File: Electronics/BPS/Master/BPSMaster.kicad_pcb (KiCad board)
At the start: 2 copper layers, 100 x 75 mm, 185 parts, among them J1 SWD, J10 DisplayJumper, J11 FrontFans, J12 BackFans, J13 ErrorLightConnector, J2 Logic Analyzer, J20 USBConnector, J21 USB_B_Micro, J3 CurrentSlaveConnector, J4 CarPowerConnector, J5 CAN_Out, J6 ContactorConnector, J7 VoltageSlaveConnector, J8 DisplayConnector, J9 TempSlaveConnector, Q1 VND5N07-E, Q2 NVR4003NT3G, Q3 NVR4003NT3G, Q4 NVR4003NT3G, SW1 B3SL-1002P, U1 STM32F413RHTx, U10 LTC6820, U11 HX1188FNL, U12 LTC6820, U13 Si8641EC-B-IS1, U14 SI8660EC-B-IS1, U15 RI3-1205S, U16 SI8261ABC-IS, U17 CP2102N-A01-GQFN24, U2 RI3-1205S, U3 NCP1117-3.3_SOT223, U4 CDSOT23-T24CAN, U5 ADM3055E, U6 BAS70-04, U7 SI8261ABC-IS, U8 M24128, U9 LSM6DS3, Y1 NX8045GB-8.000M-STD-CSJ-1

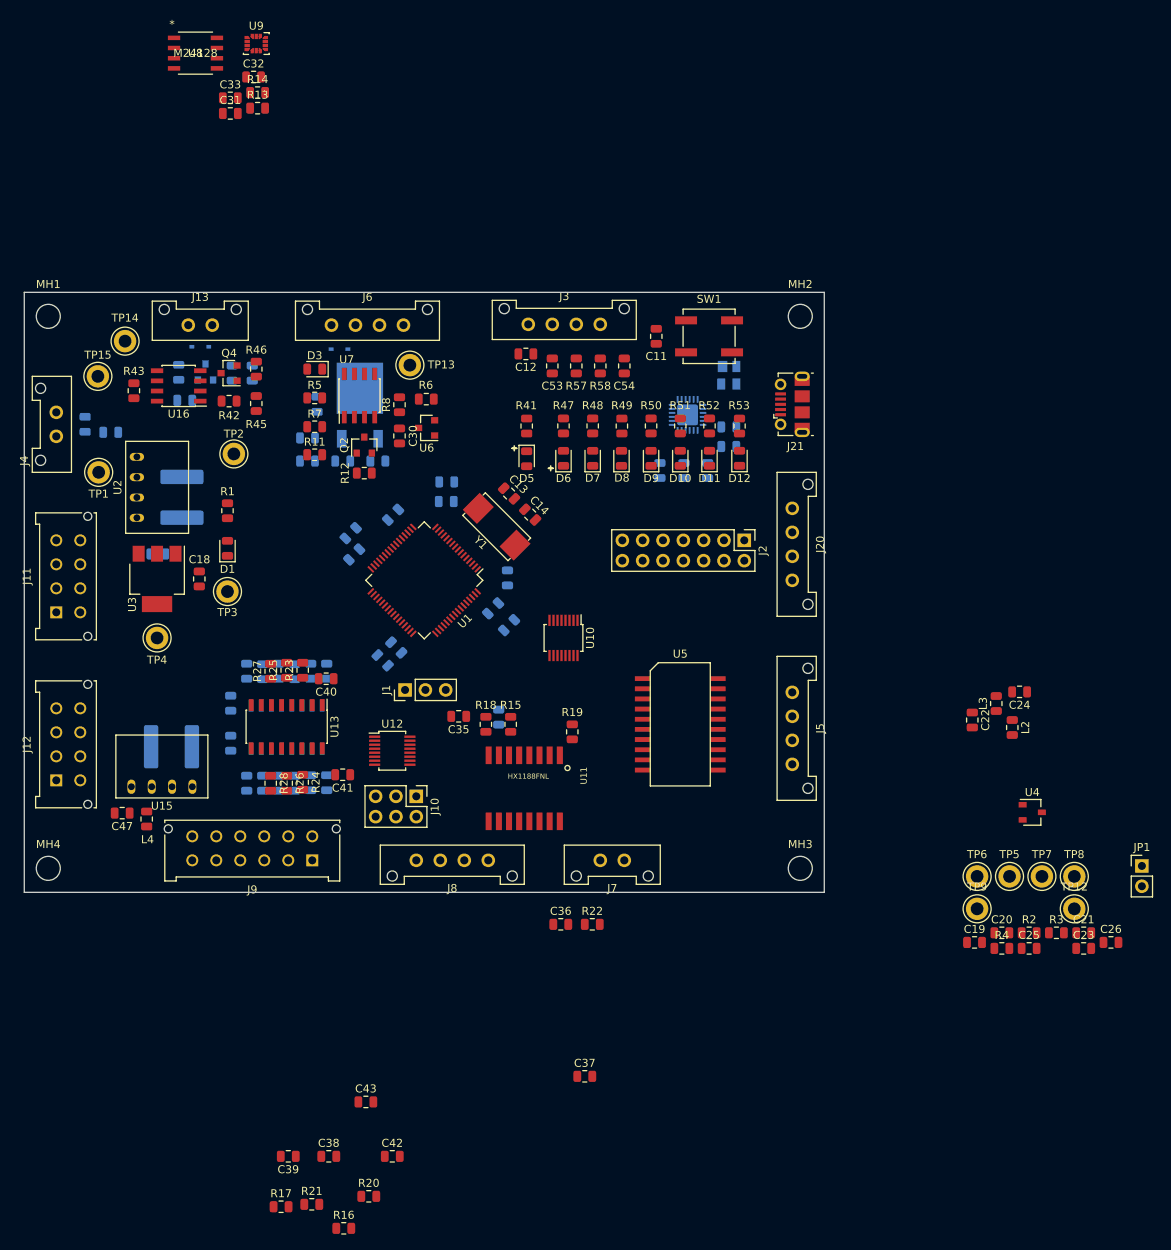
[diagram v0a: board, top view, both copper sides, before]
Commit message: Organized all components in BPS master to where they should be.
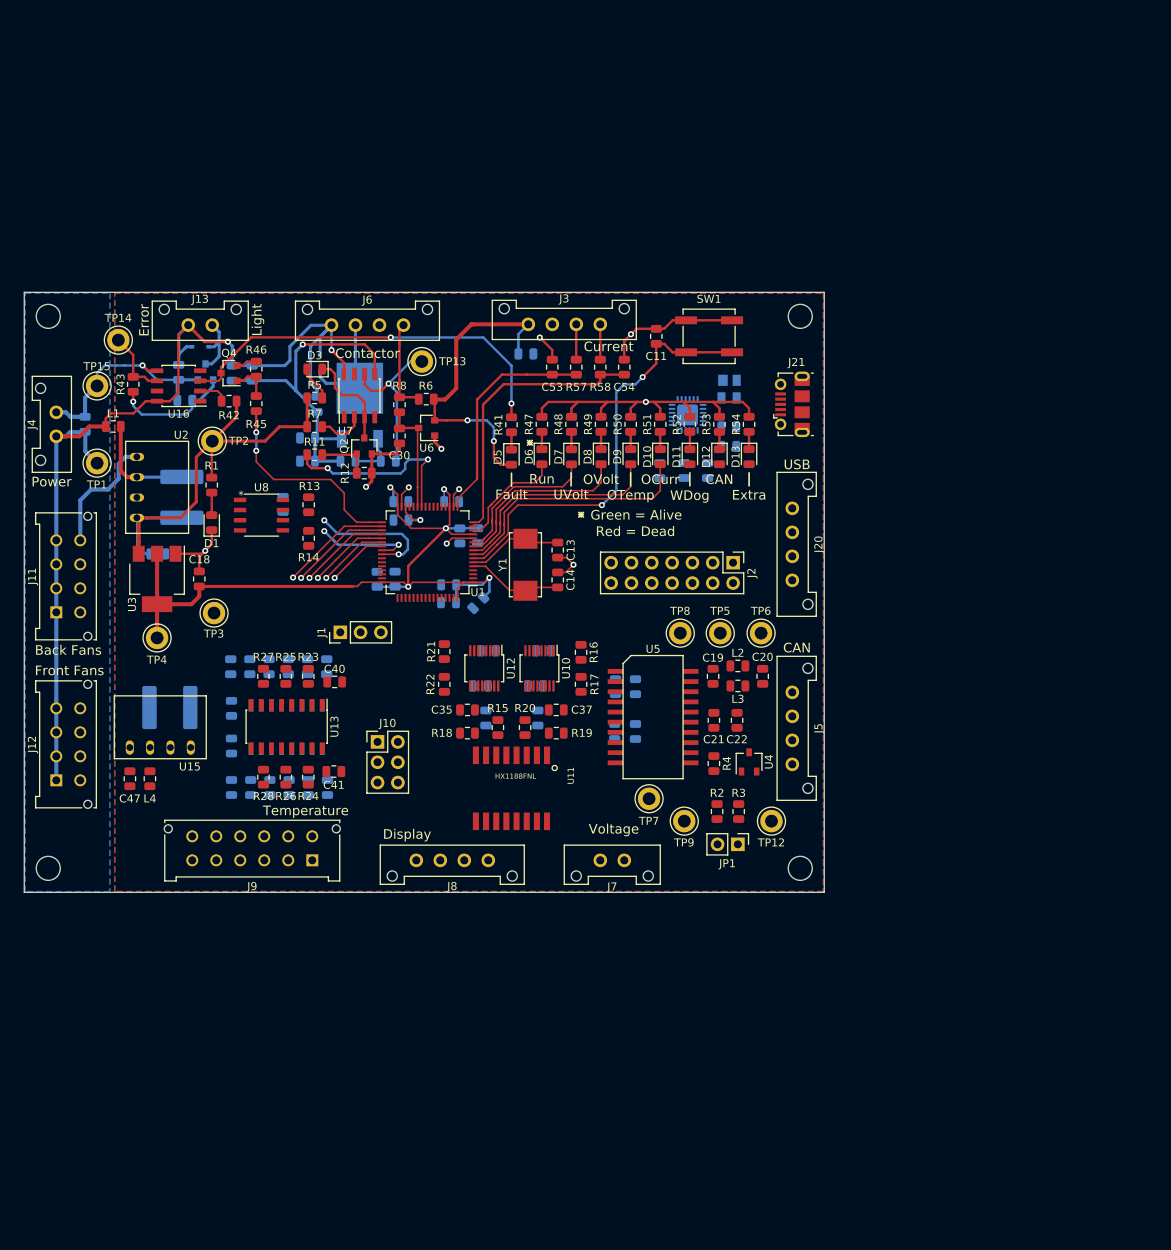
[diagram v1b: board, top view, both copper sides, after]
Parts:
- removed C32, C33: 0.1uF, Capacitor_SMD:C_0805_2012Metric
- removed U9: LSM6DS3, Package_LGA:LGA-14_3x2.5mm_P0.5mm_LayoutBorder3x4y
- added D14: SP0503BAHT, Package_TO_SOT_SMD:SOT-143, B.Cu at (188.1, 87.1)
- added R59: 1k, Resistor_SMD:R_0805_2012Metric, B.Cu at (179.4, 97.3)
- C12, C23, C24, C25, C26, C31, C36, C38, C39, C42, C43: moved to B.Cu
- D13: value SP0503BAHT -> Extra; footprint Package_TO_SOT_SMD:SOT-143 -> LED_SMD:LED_0805_2012Metric; moved to F.Cu
- D7: value OVolt -> UVolt
- D8: value UVolt -> OVolt
- L1: moved to F.Cu
- R54: value 1k -> 750; moved to F.Cu
- moved R16 77.9 mm to (169.6, 120.0), turned to 90 degrees
- moved R17 75.3 mm to (169.6, 124.0), turned to 90 degrees
- moved R21 71.1 mm to (152.5, 119.9), turned to 90 degrees
- moved C26 67.4 mm to (173.8, 129.9), turned to 270 degrees
- moved C23 67.0 mm to (173.9, 124.3), turned to 90 degrees
- moved C42 64.3 mm to (158.0, 119.8)
- moved C39 63.1 mm to (164.2, 128.2), turned to 90 degrees
- moved C38 61.8 mm to (157.0, 124.2)
- moved R20 61.8 mm to (162.6, 129.4), turned to 90 degrees
- moved U8 58.3 mm to (129.7, 102.8)
- moved TP8 57.9 mm to (182.0, 117.6)
- moved C25 56.2 mm to (176.4, 129.9), turned to 270 degrees
- moved C43 56.2 mm to (163.9, 124.2)
- moved R14 56.1 mm to (135.6, 105.8), turned to 90 degrees
- moved C21 53.3 mm to (186.2, 128.5), turned to 270 degrees
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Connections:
- net /CAN/GND_ISO_IN renamed Net-(C20-Pad2)
- net /CAN/GND_ISO_OUT renamed Net-(C19-Pad2)
- C19 pad 1: /CAN/CAN_ISA_VOUT -> Net-(C19-Pad1)
- C20 pad 1: /CAN/CAN_ISA_VOUT -> Net-(C20-Pad1)
- C21 pad 1: /CAN/CAN_ISA_VOUT -> Net-(C20-Pad1)
- C22 pad 1: /CAN/CAN_ISA_VOUT -> Net-(C20-Pad1)
- C30 pad 1: /PC7 -> /PB1
- C53 pad 1: /ADC1_CH2 -> /ADC1_CH3
- C54 pad 1: /ADC1_CH3 -> /ADC1_CH2
- D10 pad 1: GND -> Net-(D10-Pad1)
- D10 pad 2: Net-(D10-Pad2) -> /PC0
- D11 pad 1: GND -> Net-(D11-Pad1)
- D11 pad 2: Net-(D11-Pad2) -> /PA5
- D12 pad 1: GND -> Net-(D12-Pad1)
- D12 pad 2: Net-(D12-Pad2) -> /PA6
- D13 pad 1: GND -> Net-(D13-Pad1)
- D13 pad 2: /USB/VBUS -> /PA7
- D6 pad 1: GND -> Net-(D6-Pad1)
- D6 pad 2: Net-(D6-Pad2) -> /RUN
- D7 pad 1: GND -> Net-(D7-Pad1)
- D7 pad 2: Net-(D7-Pad2) -> /PC3
- D8 pad 1: GND -> Net-(D8-Pad1)
- D8 pad 2: Net-(D8-Pad2) -> /PC2
- D9 pad 1: GND -> Net-(D9-Pad1)
- D9 pad 2: Net-(D9-Pad2) -> /PC1
- J10 pad 2: /SPI/DISP_POL -> +3V3
- J10 pad 3: GND -> /SPI/DISP_POL
- J10 pad 4: +3V3 -> /SPI/DISP_PHA
- J10 pad 5: /SPI/DISP_PHA -> GND
- J5 pad 1: /CAN/CAN_ISA_VOUT -> Net-(C20-Pad1)
- J8 pad 1: +12V -> Net-(J8-Pad1)
- J8 pad 2: GNDPWR -> Net-(J8-Pad2)
- J8 pad 3: Net-(J8-Pad3) -> +12V
- J8 pad 4: Net-(J8-Pad4) -> GNDPWR
- J9 pad 5: Net-(J9-Pad5) -> GND_A
- L2 pad 1: /CAN/CAN_ISA_VOUT -> Net-(C20-Pad1)
- L2 pad 2: /CAN/CAN_ISA_VOUT -> Net-(C19-Pad1)
- R11 pad 2: /PC6 -> /PB0
- R45 pad 2: /PC1 -> /FAULT
- R47 pad 1: /PC0 -> Net-(D6-Pad1)
- R47 pad 2: Net-(D6-Pad2) -> GND
- R48 pad 1: /PC2 -> Net-(D7-Pad1)
- R48 pad 2: Net-(D7-Pad2) -> GND
- R49 pad 1: /PC3 -> Net-(D8-Pad1)
- R49 pad 2: Net-(D8-Pad2) -> GND
- R50 pad 1: /PC4 -> Net-(D9-Pad1)
- R50 pad 2: Net-(D9-Pad2) -> GND
- R51 pad 1: /PC5 -> Net-(D10-Pad1)
- R51 pad 2: Net-(D10-Pad2) -> GND
- R52 pad 1: /PA5 -> Net-(D11-Pad1)
- R52 pad 2: Net-(D11-Pad2) -> GND
- R53 pad 1: /PA6 -> Net-(D12-Pad1)
- R53 pad 2: Net-(D12-Pad2) -> GND
- R54 pad 1: +3V3 -> Net-(D13-Pad1)
- R54 pad 2: Net-(R54-Pad2) -> GND
- R57 pad 2: /ADC1_CH2 -> /ADC1_CH3
- R58 pad 2: /ADC1_CH3 -> /ADC1_CH2
- R8 pad 1: /PC7 -> /PB1
- TP5 pad 1: /CAN/CAN_ISA_VOUT -> Net-(C19-Pad1)
- TP6 pad 1: /CAN/CAN_ISA_VOUT -> Net-(C20-Pad1)
- U1 pad 14: Net-(U1-Pad14) -> /RUN
- U1 pad 23: Net-(U1-Pad23) -> /PA7
- U1 pad 26: Net-(U1-Pad26) -> /PB0
- U1 pad 27: Net-(U1-Pad27) -> /PB1
- U1 pad 29: /TEMP_CS3 -> Net-(U1-Pad29)
- U1 pad 33: /TEMP_CS4 -> /FAULT
- U1 pad 34: /TEMP_CS5 -> /TEMP_CS1
- U1 pad 35: /TEMP_CS6 -> /TEMP_CS2
- U1 pad 36: Net-(U1-Pad36) -> /TEMP_CS3
- U1 pad 37: /PC6 -> /TEMP_CS4
- U1 pad 38: /PC7 -> /TEMP_CS5
- U1 pad 39: Net-(U1-Pad39) -> /TEMP_CS6
- U1 pad 44: /CAN1_RX -> Net-(U1-Pad44)
- U1 pad 45: /CAN1_TX -> Net-(U1-Pad45)
- U1 pad 61: /TEMP_CS1 -> /CAN1_RX
- U1 pad 62: /TEMP_CS2 -> /CAN1_TX
- U11 pad 11: Net-(J8-Pad3) -> Net-(J8-Pad1)
- U11 pad 9: Net-(J8-Pad4) -> Net-(J8-Pad2)
- U17 pad 9: Net-(R54-Pad2) -> Net-(R59-Pad2)
- U5 pad 16: /CAN/CAN_ISA_VOUT -> Net-(C20-Pad1)
- U5 pad 19: /CAN/CAN_ISA_VOUT -> Net-(C19-Pad1)
- U6 pad 3: /PC7 -> /PB1
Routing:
- net +12V: track 0.00 -> 133.1 mm, vias 0 -> 2
- net +3V3: track 0.00 -> 106.6 mm, vias 0 -> 5
- net +5V: track 0.00 -> 99.4 mm, vias 0 -> 2
- net GND: track 0.00 -> 98.9 mm, vias 0 -> 10
- net GNDPWR: track 0.00 -> 86.8 mm, vias 0 -> 2
- net /NRST: track 0.00 -> 54.1 mm, vias 0 -> 2
- net Net-(Q4-Pad3): track 0.00 -> 49.8 mm, vias 0 -> 2
- net /ADC1_CH2: track 0.00 -> 35.8 mm
- net /PC0: track 0.00 -> 31.9 mm
- net /PC1: track 0.00 -> 28.3 mm
- net /ADC1_CH3: track 0.00 -> 28.1 mm
- net /FAULT: track 0.00 -> 26.5 mm, vias 0 -> 2
- net /PB0: track 0.00 -> 24.1 mm, vias 0 -> 2
- net /PC2: track 0.00 -> 23.5 mm
- net Net-(R9-Pad2): track 0.00 -> 20.5 mm, vias 0 -> 1
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- added copper zone on B.Cu, net GND
- added copper zone on F.Cu, net GND
- added copper zone on B.Cu, net GNDPWR
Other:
- net class Default: trace_width 0.1524 -> 0.3048; via_dia 0.508 -> 0.762; via_drill 0.254 -> 0.381
- board text added: "+"
- board text added: "+12V"
- board text added: "+5V"
- board text added: "+5Viso"
- board text added: "-"
- board text added: "1"
- board text added: "2"
- board text added: "3"
- board text added: "4"
- board text added: "5"
- board text added: "6"
- board text added: "AUX"
- board text added: "Back Fans"
- board text added: "CAN"
- board text added: "CANH"
- board text added: "CANL"
- board text added: "Contactor"
- board text added: "Current"
- board text added: "D+"
- board text added: "D-"
- board text added: "Display"
- board text added: "Error"
- board text added: "Extra"
- board text added: "Fault"
- board text added: "Front Fans"
- board text added: "GND"
- board text added: "GNDPWR"
- board text added: "GNDiso"
- board text added: "Green = Alive"
- board text added: "High"
- board text added: "IM"
- board text added: "IP"
- board text added: "Light"
- board text added: "Low"
- board text added: "MISO"
- board text added: "MOSI"
- board text added: "OCurr"
- board text added: "OTemp"
- board text added: "OVolt"
- board text added: "Power"
- board text added: "Red = Dead"
- board text added: "Run"
- board text added: "SCK"
- board text added: "Temperature"
- board text added: "USB"
- board text added: "UVolt"
- board text added: "VBus"
- board text added: "Voltage"
- board text added: "WDog"

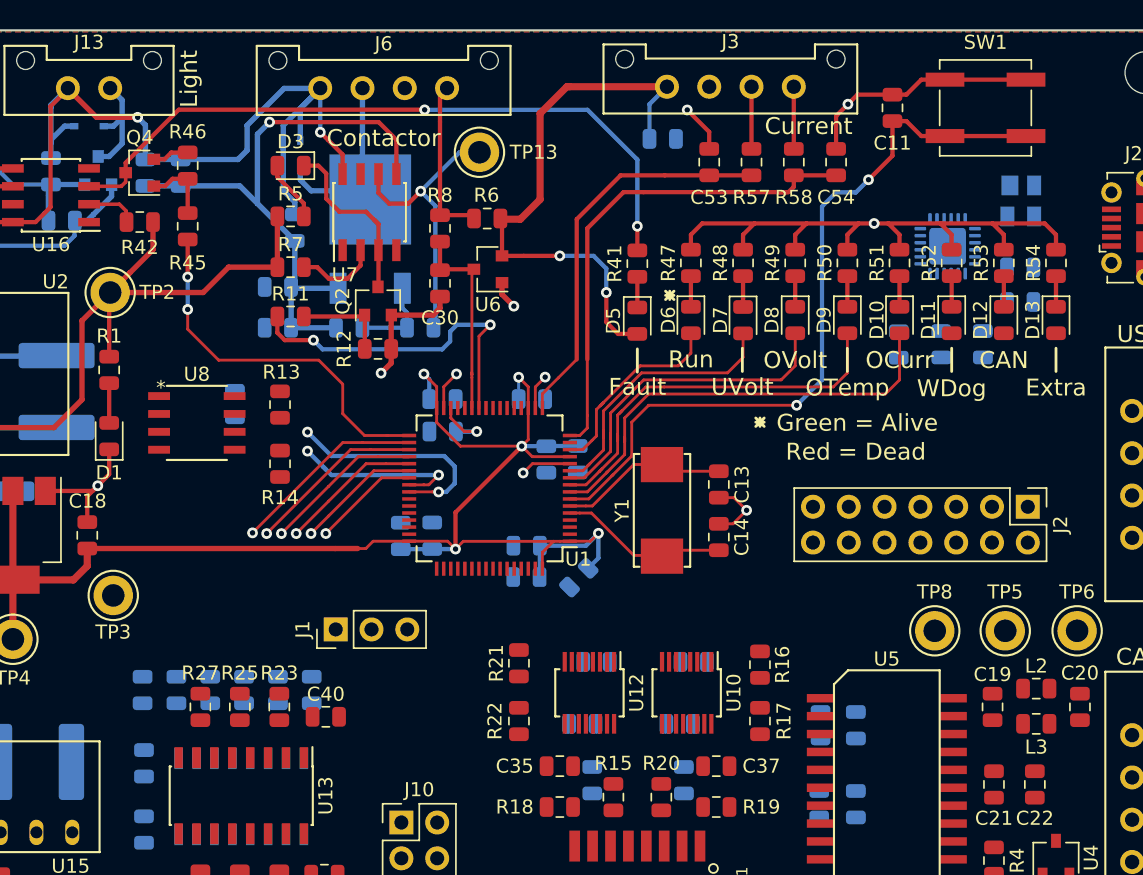
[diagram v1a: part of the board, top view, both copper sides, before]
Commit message: Traced regular GPIO pins on master board.
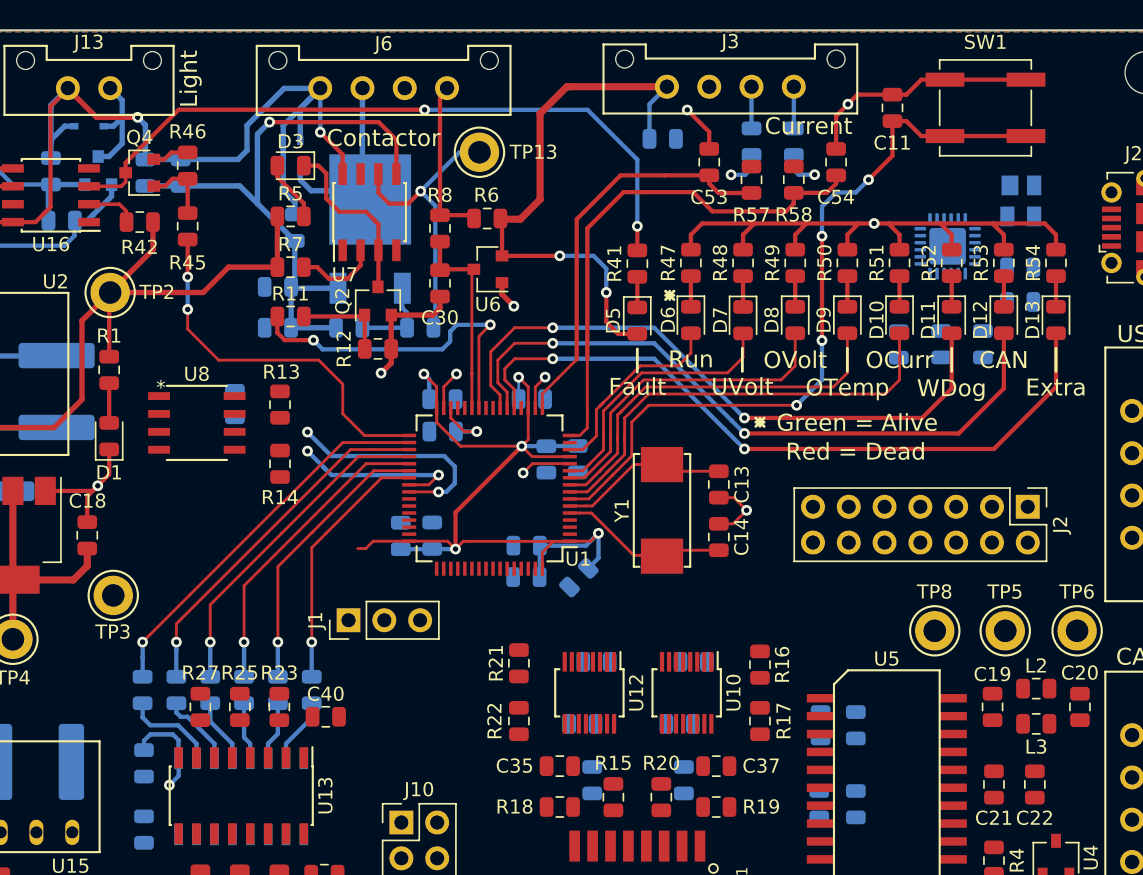
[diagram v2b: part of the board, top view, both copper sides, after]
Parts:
- added L5: 600, Inductor_SMD:L_0805_2012Metric, B.Cu at (169.0, 82.9)
- added L6: 600, Inductor_SMD:L_0805_2012Metric, B.Cu at (172.0, 82.9)
- moved R57 1.25 mm to (169.0, 85.6)
- moved R58 1.24 mm to (172.0, 85.6)
- moved J1 1.12 mm to (140.4, 116.8)
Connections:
- D11 pad 2: /PA5 -> /PA7
- D13 pad 2: /PA7 -> /PA5
- R57 pad 1: Net-(J3-Pad3) -> Net-(L5-Pad2)
- R58 pad 1: Net-(J3-Pad4) -> Net-(L6-Pad2)
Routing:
- net /PA5: track 0.00 -> 50.7 mm, vias 0 -> 2
- net /PA6: track 0.00 -> 47.9 mm, vias 0 -> 2
- net /PA7: track 0.00 -> 45.1 mm, vias 0 -> 2
- net +3V3: track 106.6 -> 87.4 mm
- net /TEMP_CS1: track 13.8 -> 27.2 mm
- net /TEMP_CS2: track 12.6 -> 25.4 mm
- net /TEMP_CS3: track 11.3 -> 23.6 mm
- net /TEMP_CS4: track 10.1 -> 21.7 mm
- net /TEMP_CS5: track 8.81 -> 20.1 mm
- net /TEMP_CS6: track 7.55 -> 18.2 mm
- net +5V: track 99.4 -> 106.3 mm, vias 2 -> 3
- net Net-(R29-Pad2): track 0.00 -> 6.65 mm
- net Net-(R31-Pad2): track 0.00 -> 5.31 mm
- net Net-(R39-Pad2): track 0.00 -> 4.66 mm
- net Net-(R33-Pad2): track 0.00 -> 4.56 mm
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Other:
- net class PowerMax: via_dia 0.508 -> 0.762; via_drill 0.254 -> 0.381
- net class SignalMax: via_dia 0.508 -> 0.762; via_drill 0.254 -> 0.381
- rule via_min_drill: 0.254 -> 0.381
- rule via_min_size: 0.508 -> 0.762
